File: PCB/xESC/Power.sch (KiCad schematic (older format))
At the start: 23 parts, among them U2 TMC6100-LA, U3 LMV321, U4 MIC5504-1.8YM5

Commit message: wip
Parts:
- added C20: CP, Capacitor_THT:CP_Radial_D8.0mm_P3.50mm, symbol Device:CP
- C1, C11, C12, C13, C2, C3, C4, C5, C6, C7, C8, C9: footprint (none) -> Capacitor_SMD:C_0805_2012Metric_Pad1.18x1.45mm_HandSolder
- C10: footprint (none) -> Capacitor_THT:CP_Radial_D8.0mm_P3.50mm
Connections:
- net GND: now also C20.2
- net U: no longer U2.5 (LSU)
- net V_M: now also C20.1
- new net LS_U: U2.5 (LSU)
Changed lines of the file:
@@
 	1    0    0    -1
 $EndComp
-Text HLabel 5350 6650 0    50   Input ~ 0
+Text HLabel 5100 6650 0    50   Input ~ 0
 V_M
 Wire Wire Line
@@
 F 0 "C4" H 2765 5496 50  0000 L CNN
 F 1 "100nF" H 2765 5405 50  0000 L CNN
-F 2 "" H 2688 5300 50  0001 C CNN
+F 2 "Capacitor_SMD:C_0805_2012Metric_Pad1.18x1.45mm_HandSolder" H 2688 5300 50  0001 C CNN
 F 3 "~" H 2650 5450 50  0001 C CNN
 	1    2650 5450
@@
 F 0 "C12" H 6665 5146 50  0000 L CNN
 F 1 "4.7uF" H 6665 5055 50  0000 L CNN
-F 2 "" H 6588 4950 50  0001 C CNN
+F 2 "Capacitor_SMD:C_0805_2012Metric_Pad1.18x1.45mm_HandSolder" H 6588 4950 50  0001 C CNN
 F 3 "~" H 6550 5100 50  0001 C CNN
 	1    6550 5100
@@
 F 0 "C1" H 2315 5496 50  0000 L CNN
 F 1 "100nF" H 2315 5405 50  0000 L CNN
-F 2 "" H 2238 5300 50  0001 C CNN
+F 2 "Capacitor_SMD:C_0805_2012Metric_Pad1.18x1.45mm_HandSolder" H 2238 5300 50  0001 C CNN
 F 3 "~" H 2200 5450 50  0001 C CNN
 	1    2200 5450
@@
 F 0 "C6" V 2798 4900 50  0000 C CNN
 F 1 "100nF@16V" V 2889 4900 50  0000 C CNN
-F 2 "" H 3088 4750 50  0001 C CNN
+F 2 "Capacitor_SMD:C_0805_2012Metric_Pad1.18x1.45mm_HandSolder" H 3088 4750 50  0001 C CNN
 F 3 "~" H 3050 4900 50  0001 C CNN
 	1    3050 4900
@@
 Wire Wire Line
 	2850 4700 2650 4700
-Wire Wire Line
-	5350 6650 5450 6650
 Text Label 5950 6650 0    50   ~ 0
 V_M
@@
 F 0 "C10" H 5568 7096 50  0000 L CNN
 F 1 "CP" H 5568 7005 50  0000 L CNN
-F 2 "" H 5488 6900 50  0001 C CNN
+F 2 "Capacitor_THT:CP_Radial_D8.0mm_P3.50mm" H 5488 6900 50  0001 C CNN
 F 3 "~" H 5450 7050 50  0001 C CNN
 	1    5450 7050
@@
 F 0 "C11" H 5865 7096 50  0000 L CNN
 F 1 "470nF" H 5865 7005 50  0000 L CNN
-F 2 "" H 5788 6900 50  0001 C CNN
+F 2 "Capacitor_SMD:C_0805_2012Metric_Pad1.18x1.45mm_HandSolder" H 5788 6900 50  0001 C CNN
 F 3 "~" H 5750 7050 50  0001 C CNN
 	1    5750 7050
@@
 F 0 "C7" H 3215 5496 50  0000 L CNN
 F 1 "100nF" H 3215 5405 50  0000 L CNN
-F 2 "" H 3138 5300 50  0001 C CNN
+F 2 "Capacitor_SMD:C_0805_2012Metric_Pad1.18x1.45mm_HandSolder" H 3138 5300 50  0001 C CNN
 F 3 "~" H 3100 5450 50  0001 C CNN
 	1    3100 5450
@@
 F 0 "C5" H 3015 3996 50  0000 L CNN
 F 1 "c?" H 3015 3905 50  0000 L CNN
-F 2 "" H 2938 3800 50  0001 C CNN
+F 2 "Capacitor_SMD:C_0805_2012Metric_Pad1.18x1.45mm_HandSolder" H 2938 3800 50  0001 C CNN
 F 3 "~" H 2900 3950 50  0001 C CNN
 	1    2900 3950
@@
 F 0 "C3" H 2765 3996 50  0000 L CNN
 F 1 "c?" H 2765 3905 50  0000 L CNN
-F 2 "" H 2688 3800 50  0001 C CNN
+F 2 "Capacitor_SMD:C_0805_2012Metric_Pad1.18x1.45mm_HandSolder" H 2688 3800 50  0001 C CNN
 F 3 "~" H 2650 3950 50  0001 C CNN
 	1    2650 3950
@@
 F 0 "C2" H 2515 3996 50  0000 L CNN
 F 1 "c?" H 2515 3905 50  0000 L CNN
-F 2 "" H 2438 3800 50  0001 C CNN
+F 2 "Capacitor_SMD:C_0805_2012Metric_Pad1.18x1.45mm_HandSolder" H 2438 3800 50  0001 C CNN
 F 3 "~" H 2400 3950 50  0001 C CNN
 	1    2400 3950
@@
 F 0 "C9" V 4952 1000 50  0000 C CNN
 F 1 "22n@100V" V 4861 1000 50  0000 C CNN
-F 2 "" H 4738 850 50  0001 C CNN
+F 2 "Capacitor_SMD:C_0805_2012Metric_Pad1.18x1.45mm_HandSolder" H 4738 850 50  0001 C CNN
 F 3 "~" H 4700 1000 50  0001 C CNN
 	1    4700 1000
@@
 F 0 "C13" H 7165 5146 50  0000 L CNN
 F 1 "2.2uF" H 7165 5055 50  0000 L CNN
-F 2 "" H 7088 4950 50  0001 C CNN
+F 2 "Capacitor_SMD:C_0805_2012Metric_Pad1.18x1.45mm_HandSolder" H 7088 4950 50  0001 C CNN
 F 3 "~" H 7050 5100 50  0001 C CNN
 	1    7050 5100
@@
 F 0 "C8" H 3865 6996 50  0000 L CNN
 F 1 "100nF" H 3865 6905 50  0000 L CNN
-F 2 "" H 3788 6800 50  0001 C CNN
+F 2 "Capacitor_SMD:C_0805_2012Metric_Pad1.18x1.45mm_HandSolder" H 3788 6800 50  0001 C CNN
 F 3 "~" H 3750 6950 50  0001 C CNN
 	1    3750 6950
@@
 	8950 1750 8300 1750
 Wire Wire Line
-	8950 1850 8950 1950
-Wire Wire Line
 	8950 1850 8300 1850
 Wire Wire Line
@@
 Text HLabel 8300 4050 0    50   Output ~ 0
 W
+$Comp
+L Device:CP C20
+U 1 1 61A2D5B8
+P 5200 7050
+F 0 "C20" H 5318 7096 50  0000 L CNN
+F 1 "CP" H 5318 7005 50  0000 L CNN
+F 2 "Capacitor_THT:CP_Radial_D8.0mm_P3.50mm" H 5238 6900 50  0001 C CNN
+F 3 "~" H 5200 7050 50  0001 C CNN
+	1    5200 7050
+	1    0    0    -1
+$EndComp
+Wire Wire Line
+	5100 6650 5200 6650
+Wire Wire Line
+	5200 6900 5200 6650
+Connection ~ 5200 6650
+Wire Wire Line
+	5200 6650 5450 6650
+Wire Wire Line
+	5200 7200 5450 7200
+Connection ~ 5450 7200
 $EndSCHEMATC

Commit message: wip
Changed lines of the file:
@@
 	4450 6150 550  6150
 $Sheet
-S 8950 2500 550  900
+S 8950 3600 550  900
 U 618D9FC1
 F0 "sheet618D9FBA" 50
+F1 "BridgeMosfets.sch" 50
+F2 "VIN" U L 8950 3750 50
+F3 "GND" U L 8950 4350 50
+F4 "PHASE" U L 8950 4050 50
+F5 "HS_GATE" I L 8950 3950 50
+F6 "LS_GATE" I L 8950 4150 50
+$EndSheet
+$Sheet
+S 8950 2500 550  900
+U 618DC168
+F0 "sheet618DC161" 50
 F1 "BridgeMosfets.sch" 50
 F2 "VIN" U L 8950 2650 50
@@
 F6 "LS_GATE" I L 8950 3050 50
 $EndSheet
-$Sheet
-S 8950 3600 550  900
-U 618DC168
-F0 "sheet618DC161" 50
-F1 "BridgeMosfets.sch" 50
-F2 "VIN" U L 8950 3750 50
-F3 "GND" U L 8950 4350 50
-F4 "PHASE" U L 8950 4050 50
-F5 "HS_GATE" I L 8950 3950 50
-F6 "LS_GATE" I L 8950 4150 50
-$EndSheet
 Wire Wire Line

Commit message: wip
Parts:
- removed C8: 100nF, Capacitor_SMD:C_0805_2012Metric_Pad1.18x1.45mm_HandSolder, symbol Device:C
- removed JP1: SolderJumper_3_Bridged12, Jumper:SolderJumper-3_P1.3mm_Bridged12_Pad1.0x1.5mm_NumberLabels, symbol Jumper:SolderJumper_3_Bridged12
- removed U4: MIC5504-1.8YM5, Package_TO_SOT_SMD:SOT-23-5_HandSoldering, symbol Regulator_Linear:MIC5504-1.8YM5
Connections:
- net 5V is gone; now on net VCC_IO: C13.1, U2.7 (5VOUT)
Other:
- note removed: "Solder Jumper to select VCCIO\nDefaults to TMC6100's 5V output.\n1 - 2: 5V\n2 - 3: 3.3V"
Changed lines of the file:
@@
 Wire Wire Line
 	2200 4600 1550 4600
-Text HLabel 1300 7250 3    50   BiDi ~ 0
-VCC_IO
 $Comp
 L Device:C C4
@@
 F6 "LS_GATE" I L 8950 1950 50
 $EndSheet
-$Comp
-L Regulator_Linear:MIC5504-1.8YM5 U4
-U 1 1 6187C01A
-P 3150 6850
-F 0 "U4" H 3150 7217 50  0000 C CNN
-F 1 "MIC5504-1.8YM5" H 3150 7126 50  0000 C CNN
-F 2 "Package_TO_SOT_SMD:SOT-23-5_HandSoldering" H 3150 6450 50  0001 C CNN
-F 3 "http://ww1.microchip.com/downloads/en/DeviceDoc/MIC550X.pdf" H 2900 7100 50  0001 C CNN
-	1    3150 6850
-	1    0    0    -1
-$EndComp
 Wire Wire Line
 	6800 5400 7050 5400
@@
 Wire Wire Line
 	5800 1750 7050 1750
-$Comp
-L Device:C C8
-U 1 1 618870BF
-P 3750 6950
-F 0 "C8" H 3865 6996 50  0000 L CNN
-F 1 "100nF" H 3865 6905 50  0000 L CNN
-F 2 "Capacitor_SMD:C_0805_2012Metric_Pad1.18x1.45mm_HandSolder" H 3788 6800 50  0001 C CNN
-F 3 "~" H 3750 6950 50  0001 C CNN
-	1    3750 6950
-	1    0    0    -1
-$EndComp
-Wire Wire Line
-	3550 6750 3750 6750
-Wire Wire Line
-	3750 6750 3750 6800
-Wire Wire Line
-	3150 7150 3150 7350
-Wire Wire Line
-	3150 7350 3750 7350
-Wire Wire Line
-	3750 7350 3750 7100
-Wire Wire Line
-	3150 7350 3150 7550
-Connection ~ 3150 7350
-$Comp
-L power:GND #PWR0107
-U 1 1 6188D671
-P 3150 7550
-F 0 "#PWR0107" H 3150 7300 50  0001 C CNN
-F 1 "GND" H 3155 7377 50  0000 C CNN
-F 2 "" H 3150 7550 50  0001 C CNN
-F 3 "" H 3150 7550 50  0001 C CNN
-	1    3150 7550
-	1    0    0    -1
-$EndComp
-Wire Wire Line
-	2750 6750 2500 6750
-Wire Wire Line
-	2750 6950 2500 6950
-Wire Wire Line
-	2500 6950 2500 6750
-Connection ~ 2500 6750
-Wire Wire Line
-	2500 6750 2300 6750
-Text Label 2300 6750 0    50   ~ 0
-5V
-$Comp
-L Jumper:SolderJumper_3_Bridged12 JP1
-U 1 1 61897811
-P 1300 6750
-F 0 "JP1" H 1300 6955 50  0000 C CNN
-F 1 "SolderJumper_3_Bridged12" H 1300 6864 50  0000 C CNN
-F 2 "Jumper:SolderJumper-3_P1.3mm_Bridged12_Pad1.0x1.5mm_NumberLabels" H 1300 6750 50  0001 C CNN
-F 3 "~" H 1300 6750 50  0001 C CNN
-	1    1300 6750
-	1    0    0    -1
-$EndComp
-Wire Wire Line
-	1300 7250 1300 7100
-Wire Wire Line
-	1300 7100 1750 7100
-Connection ~ 1300 7100
-Wire Wire Line
-	1300 7100 1300 6900
-Text Label 1750 7100 0    50   ~ 0
-VCC_IO
-Wire Wire Line
-	1100 6750 650  6750
-Wire Wire Line
-	1500 6750 1950 6750
-Wire Wire Line
-	3750 6750 4150 6750
-Connection ~ 3750 6750
-Text Label 4150 6750 0    50   ~ 0
-3V3
-Text Label 1950 6750 0    50   ~ 0
-3V3
-Text Label 650  6750 0    50   ~ 0
-5V
-Text Notes 650  6550 0    50   ~ 0
-Solder Jumper to select VCCIO\nDefaults to TMC6100's 5V output.\n1 - 2: 5V\n2 - 3: 3.3V
-Wire Notes Line
-	550  6150 550  7750
-Wire Notes Line
-	550  7750 4450 7750
-Wire Notes Line
-	4450 7750 4450 6150
-Wire Notes Line
-	4450 6150 550  6150
 $Sheet
 S 8950 3600 550  900
@@
 	2000 1400 2000 950
 Wire Wire Line
-	2200 2250 2200 950
+	2200 2250 2200 1250
 Wire Wire Line
 	2200 950  2100 950
@@
 Text HLabel 1300 3250 0    50   Input ~ 0
 WL
-Wire Wire Line
-	7050 1750 7250 1750
 Connection ~ 7050 1750
-Text HLabel 7250 1750 2    50   Output ~ 0
-5V
 Text HLabel 8300 1850 0    50   Output ~ 0
 U
@@
 	5200 7200 5450 7200
 Connection ~ 5450 7200
+Wire Wire Line
+	7050 1750 7050 700
+Wire Wire Line
+	7050 700  2750 700
+Wire Wire Line
+	2750 700  2750 1250
+Wire Wire Line
+	2750 1250 2200 1250
+Connection ~ 2200 1250
+Wire Wire Line
+	2200 1250 2200 950
+Text HLabel 2100 800  0    50   Output ~ 0
+VCC_IO
 $EndSCHEMATC

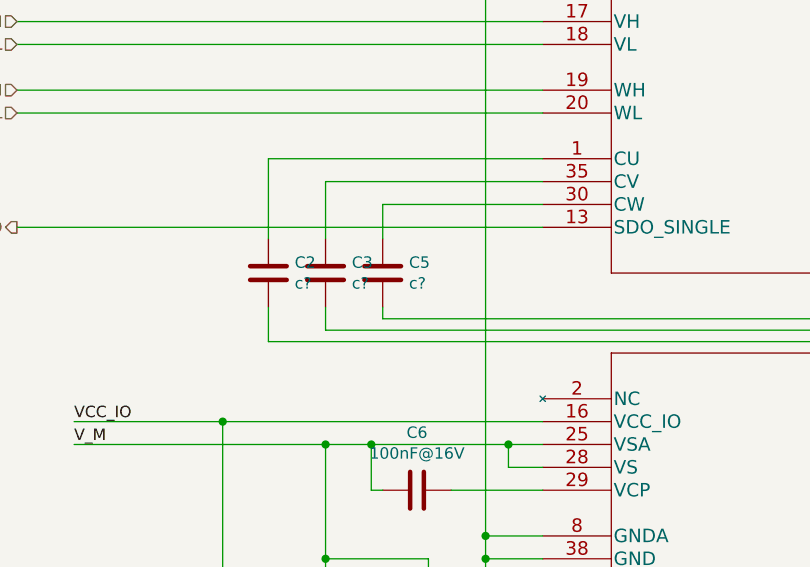
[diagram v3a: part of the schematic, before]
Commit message: added values for c2,c3,c5
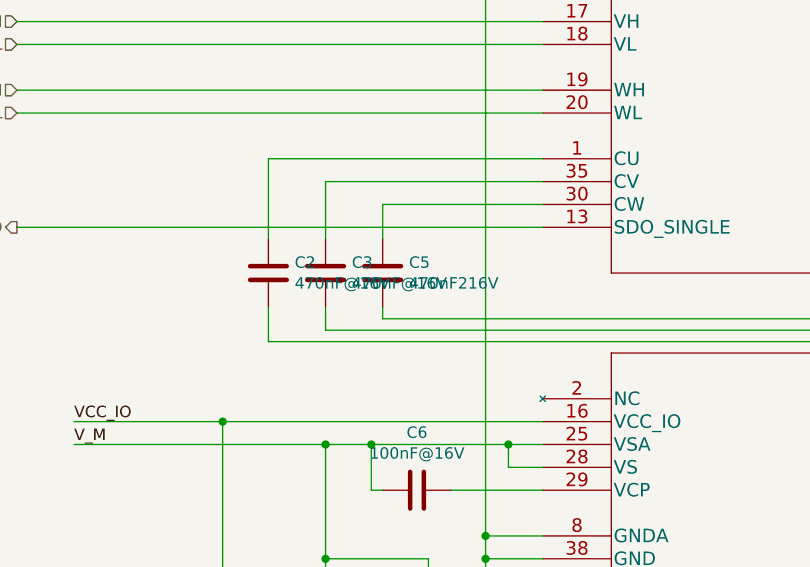
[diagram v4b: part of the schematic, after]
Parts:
- C2, C3: value c? -> 470nF@16V
- C5: value c? -> 470nF216V
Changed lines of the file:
@@
 P 2900 3950
 F 0 "C5" H 3015 3996 50  0000 L CNN
-F 1 "c?" H 3015 3905 50  0000 L CNN
+F 1 "470nF216V" H 3015 3905 50  0000 L CNN
 F 2 "Capacitor_SMD:C_0805_2012Metric_Pad1.18x1.45mm_HandSolder" H 2938 3800 50  0001 C CNN
 F 3 "~" H 2900 3950 50  0001 C CNN
@@
 P 2650 3950
 F 0 "C3" H 2765 3996 50  0000 L CNN
-F 1 "c?" H 2765 3905 50  0000 L CNN
+F 1 "470nF@16V" H 2765 3905 50  0000 L CNN
 F 2 "Capacitor_SMD:C_0805_2012Metric_Pad1.18x1.45mm_HandSolder" H 2688 3800 50  0001 C CNN
 F 3 "~" H 2650 3950 50  0001 C CNN
@@
 P 2400 3950
 F 0 "C2" H 2515 3996 50  0000 L CNN
-F 1 "c?" H 2515 3905 50  0000 L CNN
+F 1 "470nF@16V" H 2515 3905 50  0000 L CNN
 F 2 "Capacitor_SMD:C_0805_2012Metric_Pad1.18x1.45mm_HandSolder" H 2438 3800 50  0001 C CNN
 F 3 "~" H 2400 3950 50  0001 C CNN

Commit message: wip
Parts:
- C5: value 470nF216V -> 470nF@16V
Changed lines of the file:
@@
 P 2900 3950
 F 0 "C5" H 3015 3996 50  0000 L CNN
-F 1 "470nF216V" H 3015 3905 50  0000 L CNN
+F 1 "470nF@16V" H 3015 3905 50  0000 L CNN
 F 2 "Capacitor_SMD:C_0805_2012Metric_Pad1.18x1.45mm_HandSolder" H 2938 3800 50  0001 C CNN
 F 3 "~" H 2900 3950 50  0001 C CNN

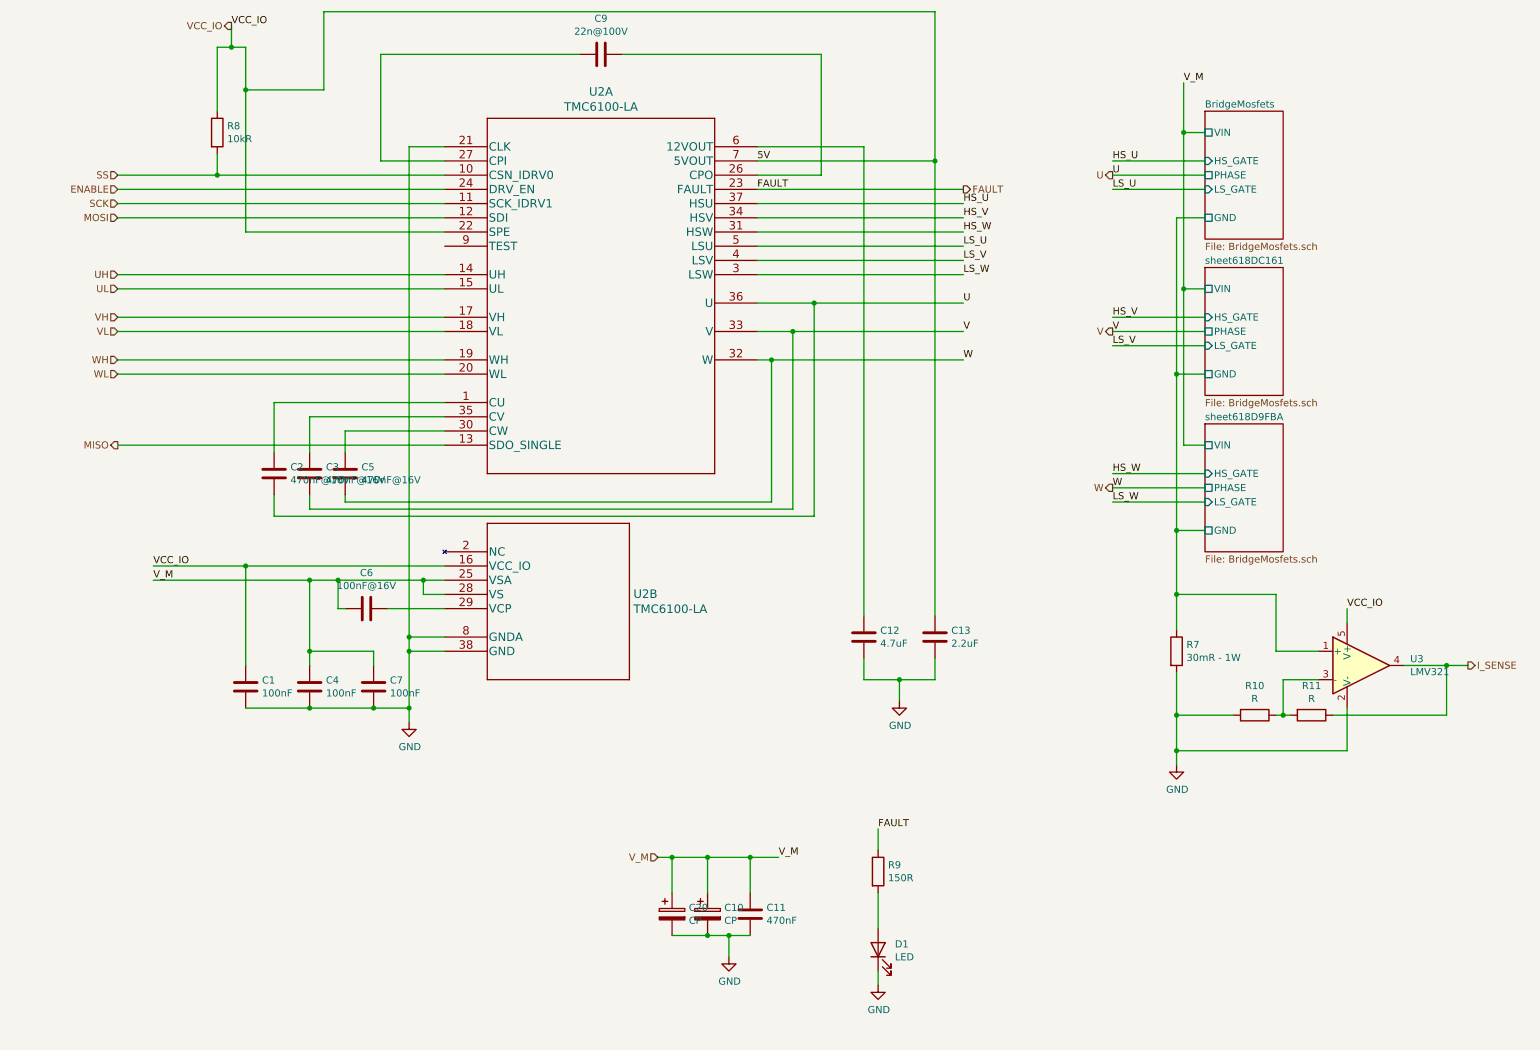
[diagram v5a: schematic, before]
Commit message: added VM to analog input, added zener diode for over voltage protection, added LED to drv_enable, shunt now 3mOhms, added jumper for TMC6100's test pin
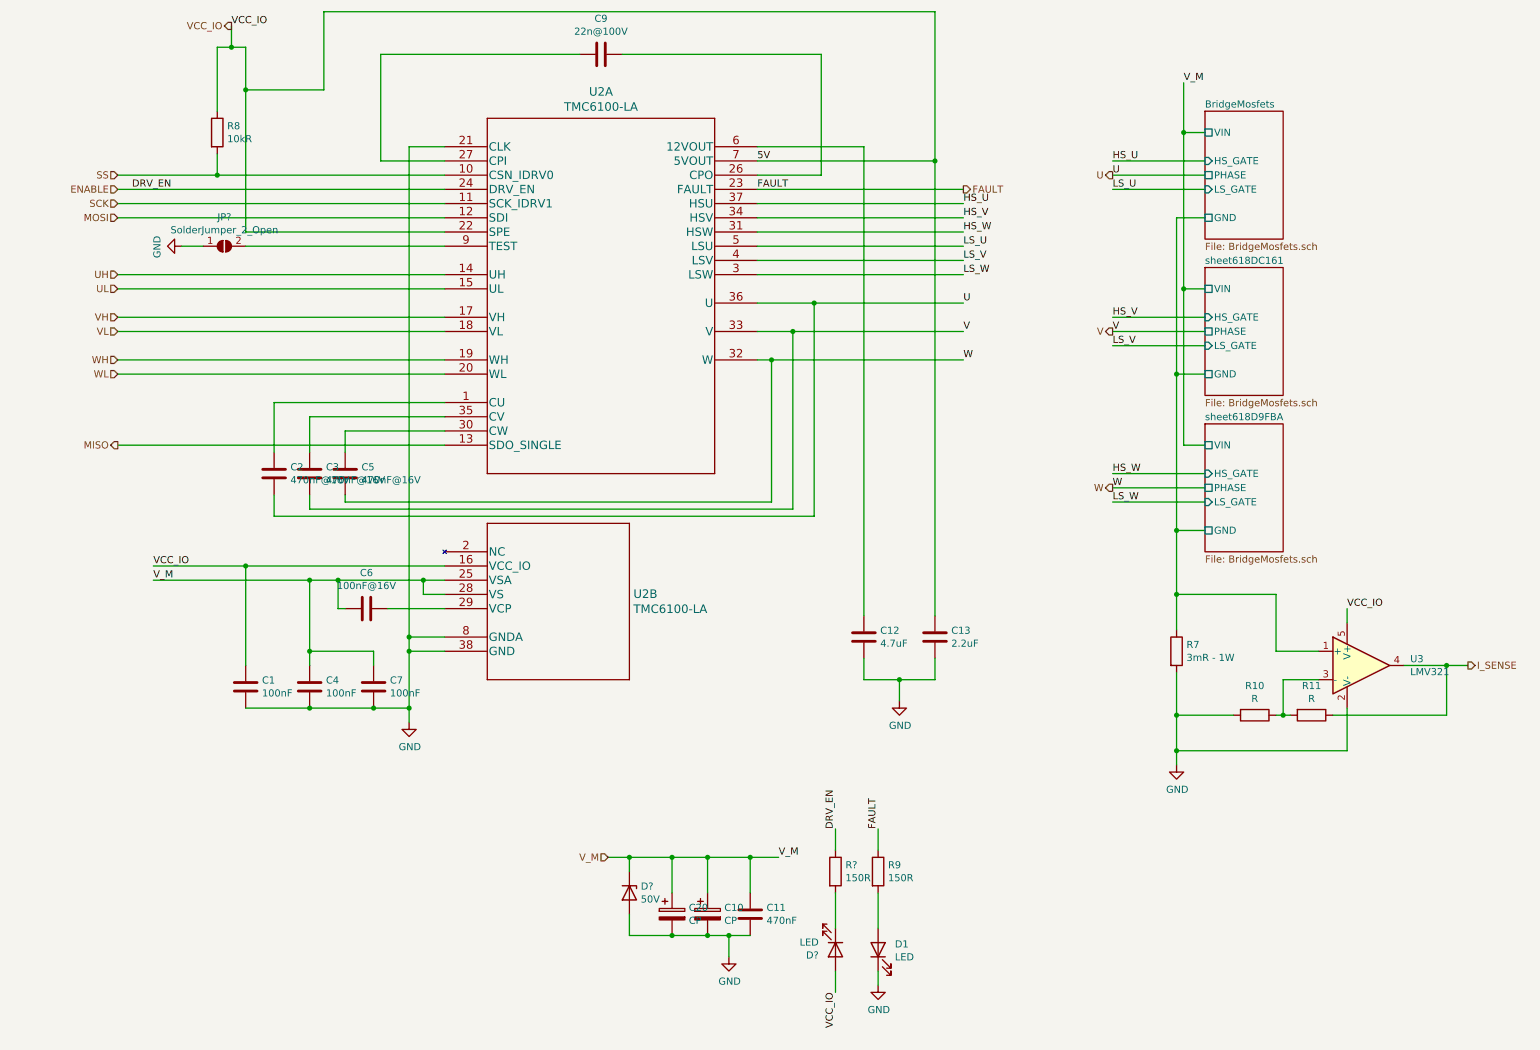
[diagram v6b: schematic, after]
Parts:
- added D?: LED, LED_SMD:LED_0805_2012Metric_Pad1.15x1.40mm_HandSolder, symbol Device:LED
- added D?: 50V, Diode_SMD:D_0805_2012Metric_Pad1.15x1.40mm_HandSolder, symbol Device:D_Zener
- added JP?: SolderJumper_2_Open, Jumper:SolderJumper-2_P1.3mm_Open_Pad1.0x1.5mm, symbol Jumper:SolderJumper_2_Open
- added R?: 150R, Resistor_SMD:R_0805_2012Metric, symbol Device:R
- R7: value 30mR - 1W -> 3mR - 1W
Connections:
- net ENABLE: now also R?.1
- net GND: now also D?.2 (A), JP?.1 (A)
- net VCC_IO: now also D?.2 (A)
- net V_M: now also D?.1 (K)
- net at U2.9 (TEST): now also JP?.2 (B)
- new net: D?.1 (K), R?.2
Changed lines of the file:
@@
 	1    0    0    -1
 $EndComp
-Text HLabel 5100 6650 0    50   Input ~ 0
+Text HLabel 4750 6650 0    50   Input ~ 0
 V_M
 Wire Wire Line
@@
 P 8750 5200
 F 0 "R7" H 8820 5246 50  0000 L CNN
-F 1 "30mR - 1W" H 8820 5155 50  0000 L CNN
+F 1 "3mR - 1W" H 8820 5155 50  0000 L CNN
 F 2 "Resistor_SMD:R_2512_6332Metric_Pad1.40x3.35mm_HandSolder" V 8680 5200 50  0001 C CNN
 F 3 "~" H 8750 5200 50  0001 C CNN
@@
 Wire Wire Line
 	6650 6600 6650 6450
-Text Label 6650 6450 0    50   ~ 0
+Text Label 6650 6450 1    50   ~ 0
 FAULT
 Wire Wire Line
@@
 $EndComp
 Wire Wire Line
-	5100 6650 5200 6650
-Wire Wire Line
 	5200 6900 5200 6650
-Connection ~ 5200 6650
 Wire Wire Line
 	5200 6650 5450 6650
@@
 Text HLabel 2100 800  0    50   Output ~ 0
 VCC_IO
+$Comp
+L Device:R R?
+U 1 1 6188DA17
+P 6350 6750
+F 0 "R?" H 6420 6796 50  0000 L CNN
+F 1 "150R" H 6420 6705 50  0000 L CNN
+F 2 "Resistor_SMD:R_0805_2012Metric" V 6280 6750 50  0001 C CNN
+F 3 "~" H 6350 6750 50  0001 C CNN
+	1    6350 6750
+	1    0    0    -1
+$EndComp
+$Comp
+L Device:LED D?
+U 1 1 6188DA1D
+P 6350 7300
+F 0 "D?" V 6389 7182 50  0000 R CNN
+F 1 "LED" V 6298 7182 50  0000 R CNN
+F 2 "LED_SMD:LED_0805_2012Metric_Pad1.15x1.40mm_HandSolder" H 6350 7300 50  0001 C CNN
+F 3 "~" H 6350 7300 50  0001 C CNN
+	1    6350 7300
+	0    1    1    0
+$EndComp
+Wire Wire Line
+	6350 7150 6350 6900
+Wire Wire Line
+	6350 6600 6350 6450
+Wire Wire Line
+	6350 7450 6350 7600
+Text Label 6350 7600 3    50   ~ 0
+VCC_IO
+Text Label 1400 1950 0    50   ~ 0
+DRV_EN
+Text Label 6350 6450 1    50   ~ 0
+DRV_EN
+Wire Wire Line
+	3600 2350 2200 2350
+$Comp
+L Jumper:SolderJumper_2_Open JP?
+U 1 1 618B45F2
+P 2050 2350
+F 0 "JP?" H 2050 2555 50  0000 C CNN
+F 1 "SolderJumper_2_Open" H 2050 2464 50  0000 C CNN
+F 2 "Jumper:SolderJumper-2_P1.3mm_Open_Pad1.0x1.5mm" H 2050 2350 50  0001 C CNN
+F 3 "~" H 2050 2350 50  0001 C CNN
+	1    2050 2350
+	1    0    0    -1
+$EndComp
+Wire Wire Line
+	1900 2350 1750 2350
+$Comp
+L power:GND #PWR?
+U 1 1 618B6034
+P 1750 2350
+F 0 "#PWR?" H 1750 2100 50  0001 C CNN
+F 1 "GND" H 1755 2177 50  0000 C CNN
+F 2 "" H 1750 2350 50  0001 C CNN
+F 3 "" H 1750 2350 50  0001 C CNN
+	1    1750 2350
+	0    1    1    0
+$EndComp
+Wire Wire Line
+	4750 6650 4900 6650
+Connection ~ 5200 6650
+$Comp
+L Device:D_Zener D?
+U 1 1 618C9F81
+P 4900 6900
+F 0 "D?" V 4854 6980 50  0000 L CNN
+F 1 "50V" V 4945 6980 50  0000 L CNN
+F 2 "Diode_SMD:D_0805_2012Metric_Pad1.15x1.40mm_HandSolder" H 4900 6900 50  0001 C CNN
+F 3 "~" H 4900 6900 50  0001 C CNN
+	1    4900 6900
+	0    1    1    0
+$EndComp
+Wire Wire Line
+	4900 6750 4900 6650
+Connection ~ 4900 6650
+Wire Wire Line
+	4900 6650 5200 6650
+Wire Wire Line
+	4900 7050 4900 7200
+Wire Wire Line
+	4900 7200 5200 7200
+Connection ~ 5200 7200
 $EndSCHEMATC
